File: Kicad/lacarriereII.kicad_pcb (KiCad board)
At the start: 2 copper layers, 92 x 92 mm, 74 parts, among them J1 USB_C_Receptacle_USB2.0, J2 Conn_02x06, J4 Conn_01x06_Pin, U1 PCA9557PW, U10 XC6206P132MR, U11 ESP32_WROVER, U13 BME280, U15 BME280, U2 BQ25171QWDRCRQ1, U3 CH340C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

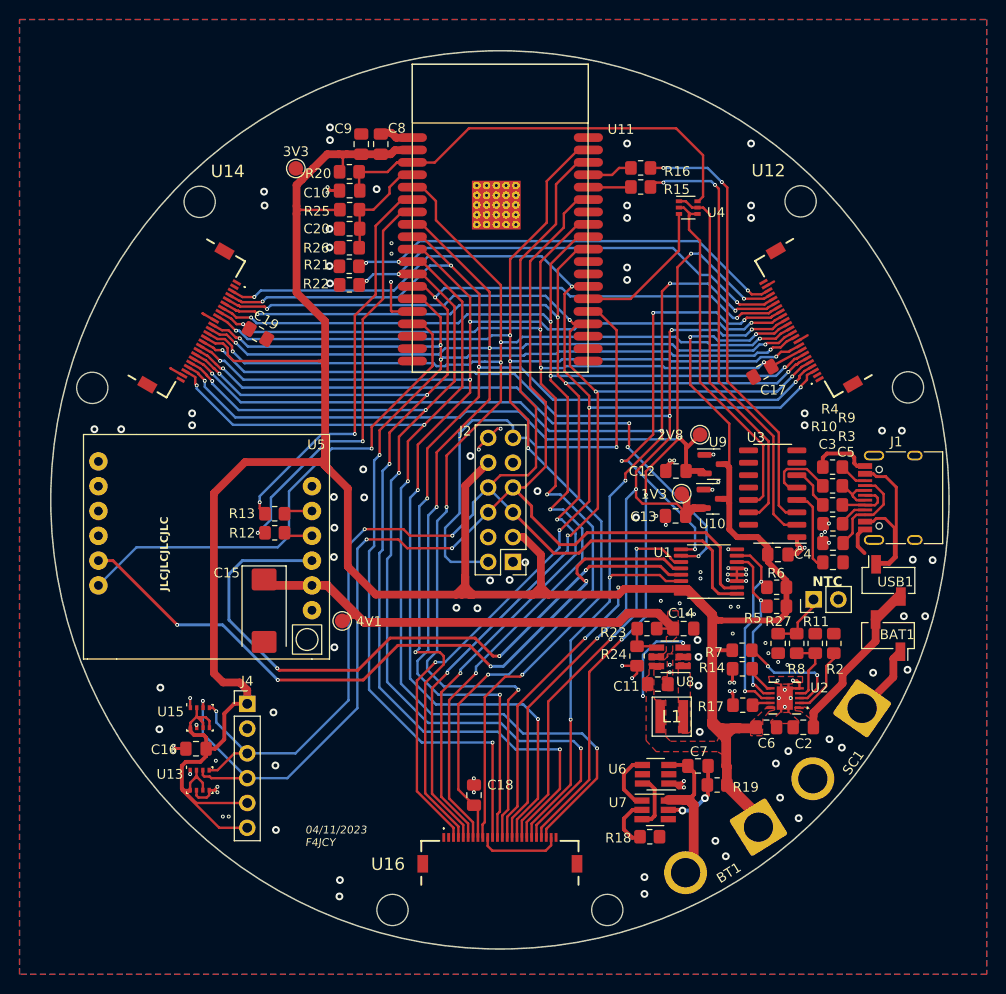
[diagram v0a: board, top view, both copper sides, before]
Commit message: [change] ov2640 footprint and add BOM
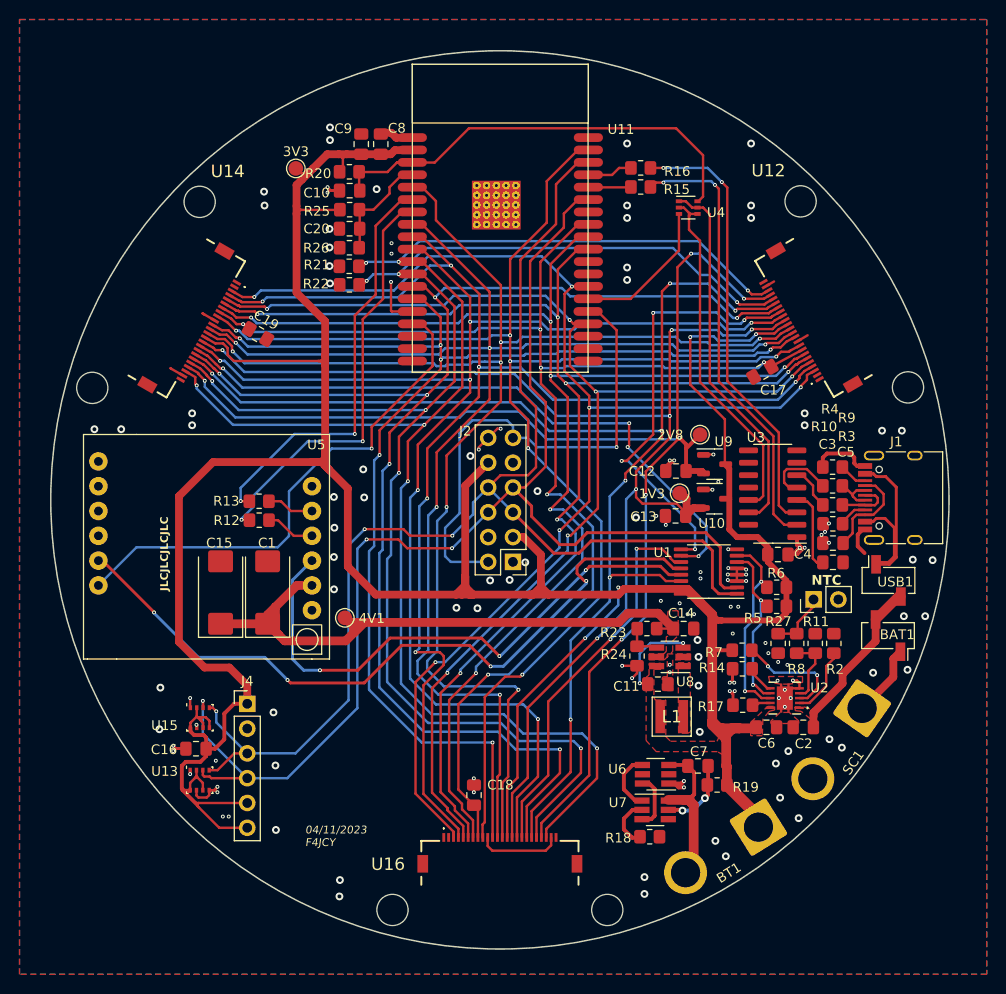
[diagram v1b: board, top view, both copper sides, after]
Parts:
- added C1: NC(100u), Capacitor_Tantalum_SMD:CP_EIA-7343-31_Kemet-D_Pad2.25x2.55mm_HandSolder, F.Cu at (76.2, 109.5)
- R12, R13: value R0 -> 0R
- R2: value 375R -> 750R
- U10, U9: footprint Package_TO_SOT_SMD:SOT-23 -> Package_TO_SOT_SMD:SOT-23-3
- moved C15 4.83 mm to (71.4, 109.5), turned to 90 degrees
- moved R13 2.05 mm to (75.3, 100.1)
- moved R12 2.05 mm to (75.3, 102.1)
- moved 4V1 0.42 mm to (84.1, 112.1)
- moved 1V3 0.21 mm to (118.4, 99.3)
- moved U10 0.16 mm to (122.0, 99.9)
- moved U9 0.08 mm to (122.0, 96.3)
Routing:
- net +4V: track 48.7 -> 66.1 mm
- net /GSM_RESET: track 68.5 -> 57.5 mm
- net +3.3V: track 362.8 -> 368.0 mm
- net Net-(U5-RXD): track 2.94 -> 5.06 mm
- net Net-(U5-TXD): track 2.93 -> 4.82 mm
- net /GSM_RX: track 41.4 -> 43.3 mm
- net /GSM_TX: track 42.9 -> 43.5 mm
